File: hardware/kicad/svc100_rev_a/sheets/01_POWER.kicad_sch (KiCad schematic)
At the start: 0 parts

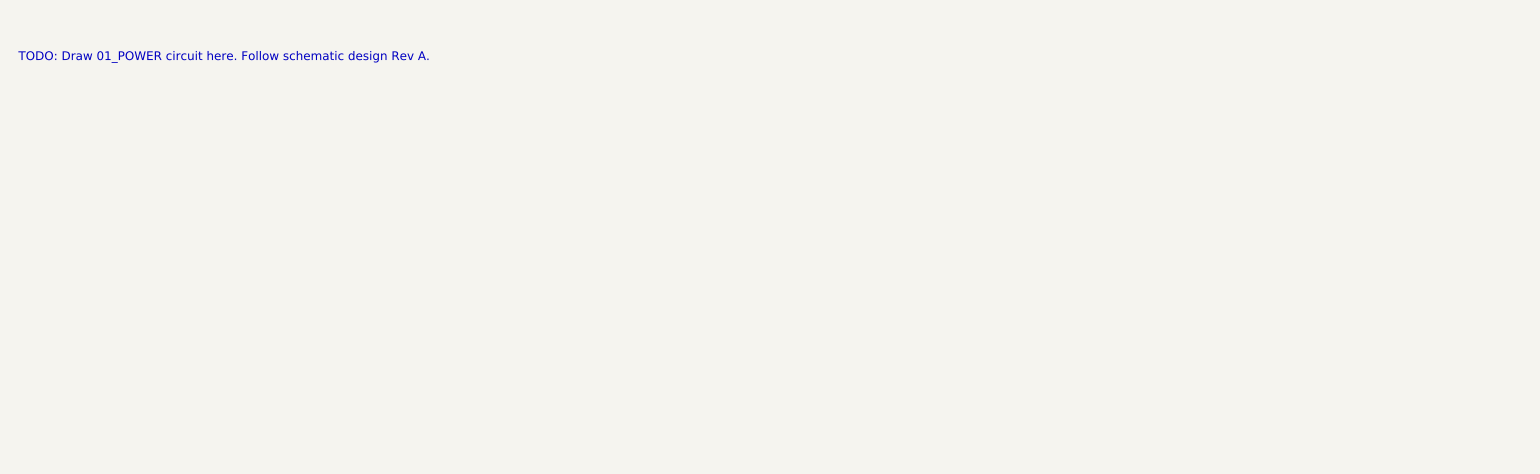
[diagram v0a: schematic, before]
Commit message: docs+hw: bible/security/coding/HAL standards, Rev A power sheet, UI simulator v2, task queue
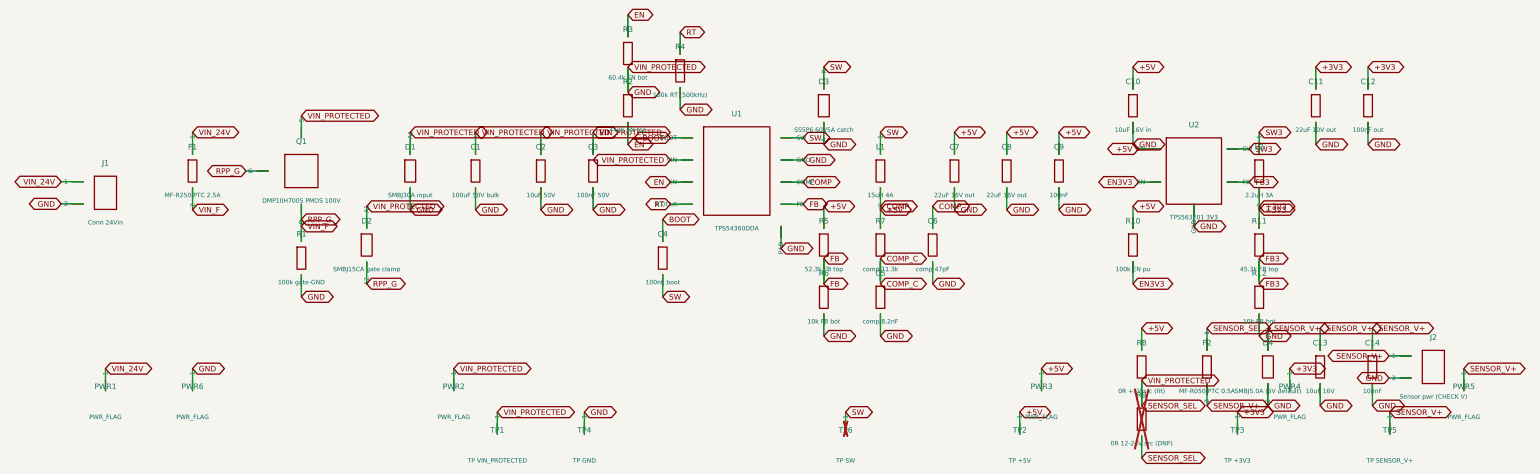
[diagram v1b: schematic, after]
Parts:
- added C1: 100uF 50V bulk, Capacitor_SMD:CP_Elec_8x10.5, symbol svc:CP
- added C10: 10uF 16V in, Capacitor_SMD:C_0805_2012Metric, symbol svc:C
- added C11: 22uF 10V out, Capacitor_SMD:C_0805_2012Metric, symbol svc:C
- added C12: 100nF out, Capacitor_SMD:C_0603_1608Metric, symbol svc:C
- added C13: 10uF 16V, Capacitor_SMD:C_1210_3225Metric, symbol svc:C
- added C14, C9: 100nF, Capacitor_SMD:C_0603_1608Metric, symbol svc:C
- added C2: 10uF 50V, Capacitor_SMD:C_1210_3225Metric, symbol svc:C
- added C3: 100nF 50V, Capacitor_SMD:C_0603_1608Metric, symbol svc:C
- added C4: 100nF boot, Capacitor_SMD:C_0603_1608Metric, symbol svc:C
- added C5: comp 8.2nF, Capacitor_SMD:C_0603_1608Metric, symbol svc:C
- added C6: comp 47pF, Capacitor_SMD:C_0603_1608Metric, symbol svc:C
- added C7, C8: 22uF 16V out, Capacitor_SMD:C_1210_3225Metric, symbol svc:C
- added D1: SMBJ30A input, Diode_SMD:D_SMB, symbol svc:TVS
- added D2: SMBJ15CA gate clamp, Diode_SMD:D_SMB, symbol svc:TVS
- added D3: SS5P6 60V5A catch, Diode_SMD:D_SMC, symbol svc:DIODE
- added D4: SMBJ5.0A (5V default), Diode_SMD:D_SMB, symbol svc:TVS
- added F1: MF-R250 PTC 2.5A, Fuse:Fuse_Bourns_MF-RG300, symbol svc:FUSE
- added F2: MF-R050 PTC 0.5A, Fuse:Fuse_Bourns_MF-RG300, symbol svc:FUSE
- added J1: Conn 24Vin, TerminalBlock:TerminalBlock_bornier-2_P5.08mm, symbol svc:SCREW2
- added J2: Sensor pwr (CHECK V), TerminalBlock:TerminalBlock_bornier-2_P5.08mm, symbol svc:SCREW2
- added L1: 15uH 4A, Inductor_SMD:L_Bourns-SRP1245A, symbol svc:L
- added L2: 2.2uH 3A, Inductor_SMD:L_Bourns-SRP6540, symbol svc:L
- added PWR1, PWR2, PWR3, PWR4, PWR5, PWR6: PWR_FLAG, symbol svc:FLAG
- added Q1: DMP10H700S PMOS 100V, Package_TO_SOT_SMD:SOT-23, symbol svc:PMOS
- added R1: 100k gate-GND, Resistor_SMD:R_0603_1608Metric, symbol svc:R
- added R10: 100k EN pu, Resistor_SMD:R_0603_1608Metric, symbol svc:R
- added R11: 45.3k FB top, Resistor_SMD:R_0603_1608Metric, symbol svc:R
- added R12, R6: 10k FB bot, Resistor_SMD:R_0603_1608Metric, symbol svc:R
- added R2: 442k EN top, Resistor_SMD:R_0603_1608Metric, symbol svc:R
- added R3: 60.4k EN bot, Resistor_SMD:R_0603_1608Metric, symbol svc:R
- added R4: 100k RT (500kHz), Resistor_SMD:R_0603_1608Metric, symbol svc:R
- added R5: 52.3k FB top, Resistor_SMD:R_0603_1608Metric, symbol svc:R
- added R7: comp 11.3k, Resistor_SMD:R_0603_1608Metric, symbol svc:R
- added R8: 0R +5V src (fit), Resistor_SMD:R_0603_1608Metric, symbol svc:R
- added R9: 0R 12-24V src (DNP), Resistor_SMD:R_0603_1608Metric, symbol svc:R
- added TP1: TP VIN_PROTECTED, TestPoint:TestPoint_Pad_D2.0mm, symbol svc:TP
- added TP2: TP +5V, TestPoint:TestPoint_Pad_D2.0mm, symbol svc:TP
- added TP3: TP +3V3, TestPoint:TestPoint_Pad_D2.0mm, symbol svc:TP
- added TP4: TP GND, TestPoint:TestPoint_Pad_D2.0mm, symbol svc:TP
- added TP5: TP SENSOR_V+, TestPoint:TestPoint_Pad_D2.0mm, symbol svc:TP
- added TP6: TP SW, TestPoint:TestPoint_Pad_D2.0mm, symbol svc:TP
- added U1: TPS54360DDA, Package_SO:HSOP-8-1EP_3.9x4.9mm, symbol svc:BUCK
- added U2: TPS563201 3V3, Package_TO_SOT_SMD:SOT-23-6, symbol svc:BUCK33
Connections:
- new net +3V3: C11.1, C12.1, L2.2, PWR4.1, R11.1, TP3.1
- new net +5V: C10.1, C6.1, C7.1, C8.1, C9.1, L1.2, PWR3.1, R10.1, R5.1, R7.1, R8.1, TP2.1, U1.6 (COMP), U2.3 (VIN)
- new net BOOT: C4.1, U1.1 (BOOT)
- new net COMP_C: C5.1, R7.2
- new net EN: R2.2, R3.1, U1.3 (EN)
- new net EN3V3: R10.2, U2.5 (EN)
- new net FB: R5.2, R6.1, U1.5 (FB)
- new net FB3: R11.2, R12.1, U2.4 (FB)
- new net GND: C1.1 (+), C1.2 (-), C10.2, C11.2, C12.2, C13.2, C14.2, C2.1, C2.2, C3.1, C3.2, C5.2, C6.2, C7.2, C8.2, C9.2, D1.1 (A1), D1.2 (A2), D2.1 (A1), D3.2 (A), D4.2 (A2), F2.1, J1.2, J2.2, PWR2.1, PWR6.1, Q1.2 (S), R1.2, R12.2, R2.1, R3.2, R4.2, R6.2, R8.2, R9.1, R9.2, TP1.1, TP4.1, U1.2 (VIN), U1.7 (GND), U1.9 (PAD), U2.1 (GND)
- new net RPP_G: D2.2 (A2), F1.2, Q1.1 (G), Q1.3 (D), R1.1
- new net RT: R4.1, U1.4 (RT/CLK)
- new net SENSOR_V+: C13.1, C14.1, D4.1 (A1), F2.2, J2.1, PWR5.1, TP5.1
- new net SW: C4.2, D3.1 (K), L1.1, TP6.1, U1.8 (SW)
- new net SW3: L2.1, U2.2 (SW)
- new net VIN_24V: F1.1, J1.1, PWR1.1
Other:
- note removed: "TODO: Draw 01_POWER circuit here. Follow schematic design Rev A."
- company: CNX Smart Home / Smart Villa OS -> Smart Villa OS
- title: SVC-100 Pro Rev A - 01_POWER -> SVC-100 Rev A - 01 POWER
